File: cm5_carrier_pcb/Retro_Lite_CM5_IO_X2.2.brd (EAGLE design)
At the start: 82.7 x 91.3 mm, 317 parts, among them J1 5025700893, J10 5051100892, J11 1072TR, J12 5034802000, J13 5040500491, J14 5051100492, J2 SJ-43516-SMT, J4 5051100492, J5 685119136923, J6 5034802000, J7 105450-0101, J8 MDT320E01001, J9 5051103091, Q1 AO3400A, Q2 AO3400A, Q3 AO3400A, Q4 AO3400A, Q5 AO3400A, Q6 AO3400A, Q7 AO3400A, Q8 AO3400A, Q9 AO3400A, U10 UM3204QQFN14_3.5X3.5_UM3204_U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, U11 MAX17055ETB+T, U12 SY8089AAACSY8089AAAC_SGY-L, U13 UM3204QQFN14_3.5X3.5_UM3204_U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, U14 MCU-ATTINY84A-MU(QFN20), U16 TPS61160ADRVT, U18 TSIC_306_SOP-8, U19 SN74LVC1G17DCKR, U2 TPD4E05U06DQAR, U20 SN74LVC1G17DCKR, U21 TPS65987DDHRSHR, U22 TPD4E05U06DQAR, U23 TUSB546-DCIRNQT, U24 TPD4E05U06DQAR, U3 TPD4E05U06DQAR, U4 W25X05CLUXIGTR, U5 BQ24292I, U6 WM8960, U7 TPS61235PRWLT, U8 UM3204QQFN14_3.5X3.5_UM3204_U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, U9 UM3204QQFN14_3.5X3.5_UM3204_U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, Y1 ECS-3225MV-240-BN-TR, Y2 ECS-.327-12.5-12R-TR

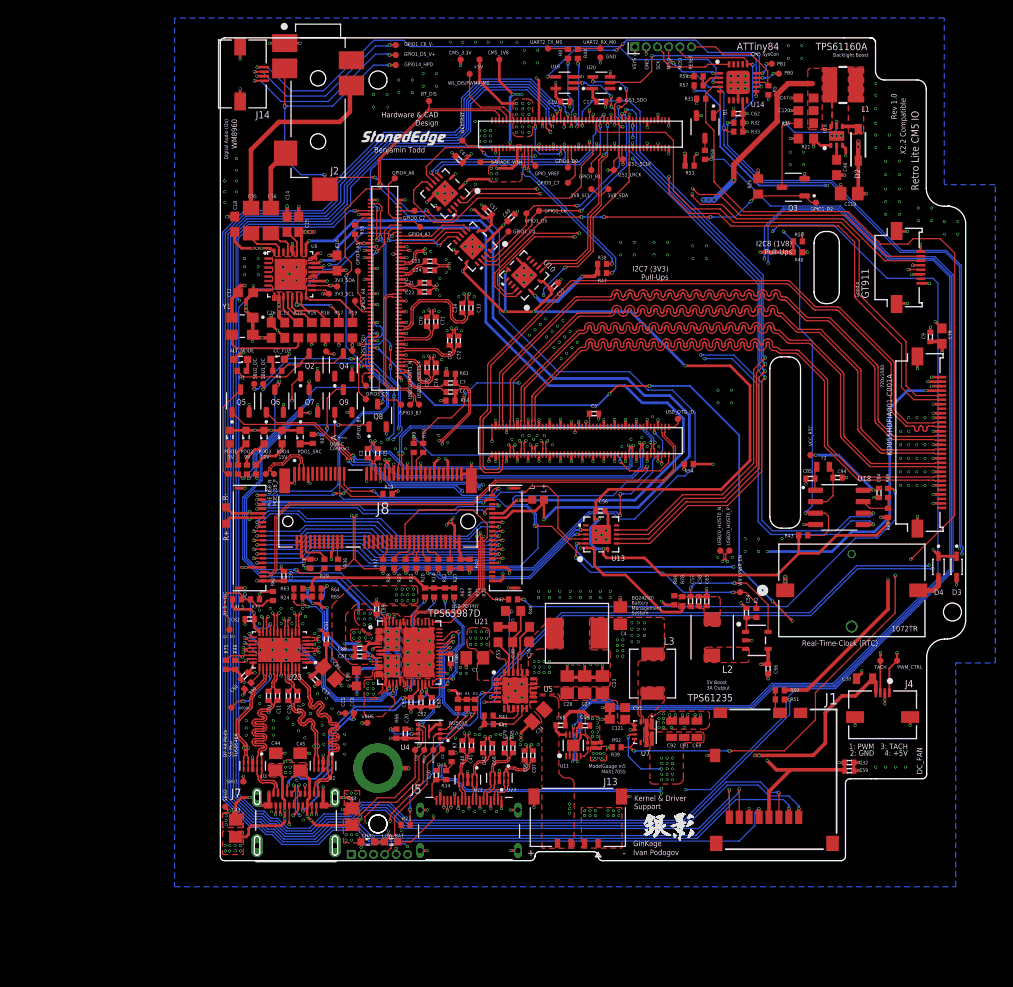
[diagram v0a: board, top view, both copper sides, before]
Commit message: Fix M.2 standoff hole size for 9774015243R
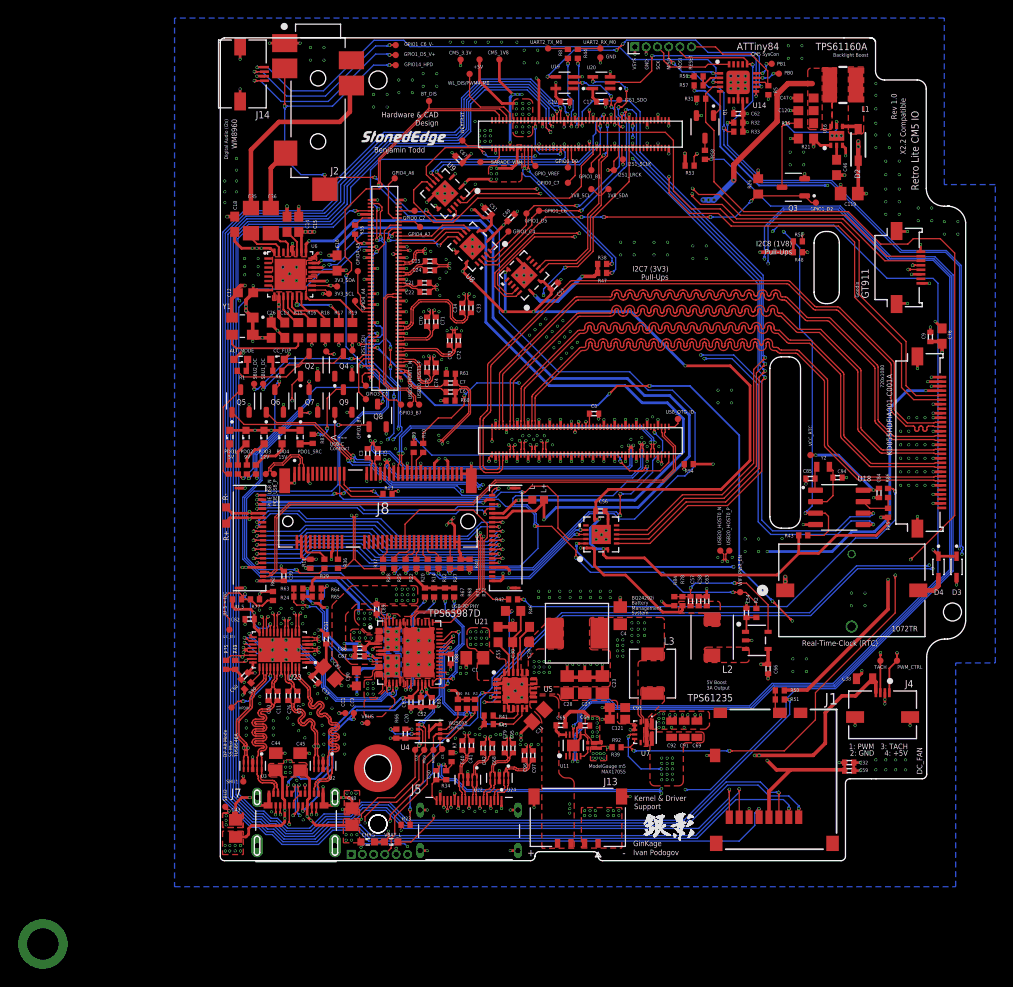
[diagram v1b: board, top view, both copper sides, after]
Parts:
- added H1: M2 x 1.5mm, Eagle_WA-SMSI (rev21a):WA-SMSI_9774015243
- moved U$7 42.0 mm to (-29.1, -12.8), flipped to the bottom
- moved R84 0.10 mm to (40.9, 25.2)
- renumbered LOW_BAT to VBAT_L
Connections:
- net GND: now also H1.1; no longer U$7.P$1
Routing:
- net GND: track 304.1 -> 300.5 mm, vias 554 -> 557

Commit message: Add files via upload
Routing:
- net GND: track 300.5 -> 303.5 mm, vias 557 -> 562

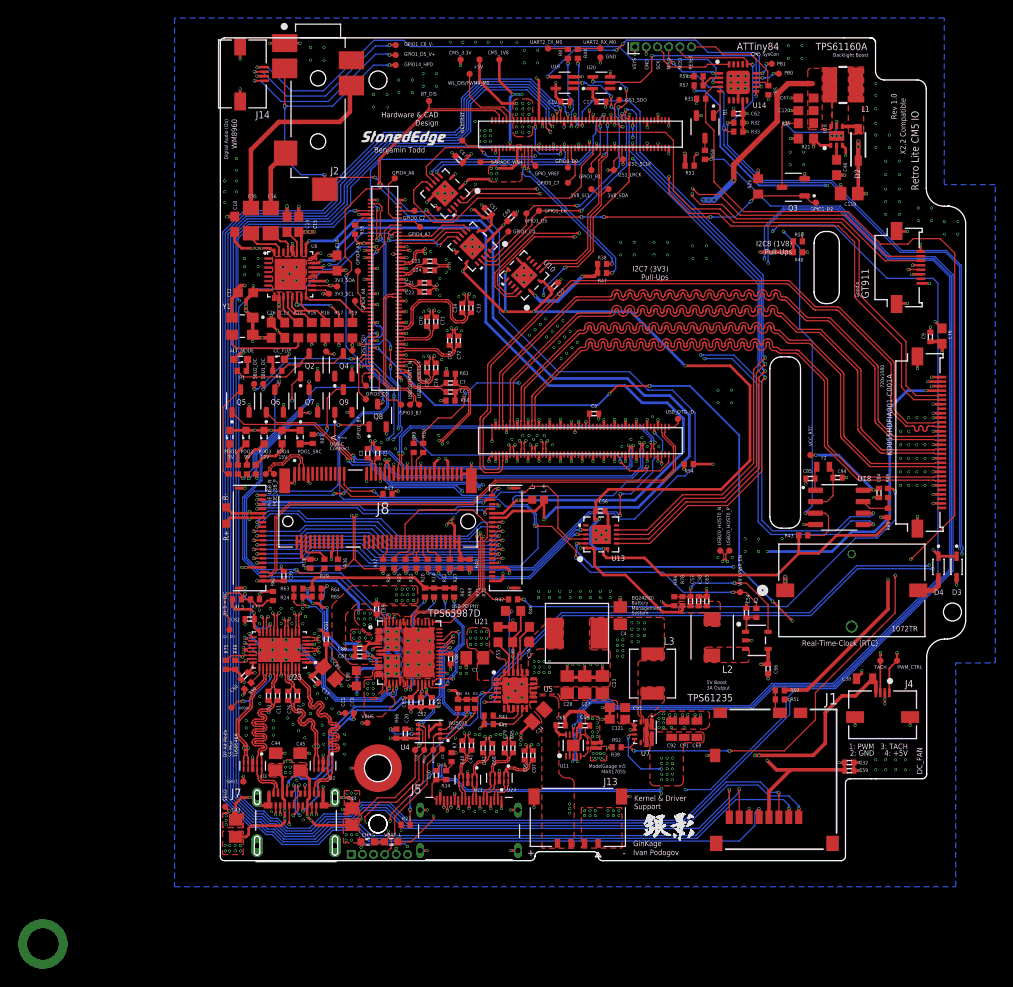
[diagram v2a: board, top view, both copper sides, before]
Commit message: Add BG_STAT, PG_GOOD pins to CM5 GPIOs
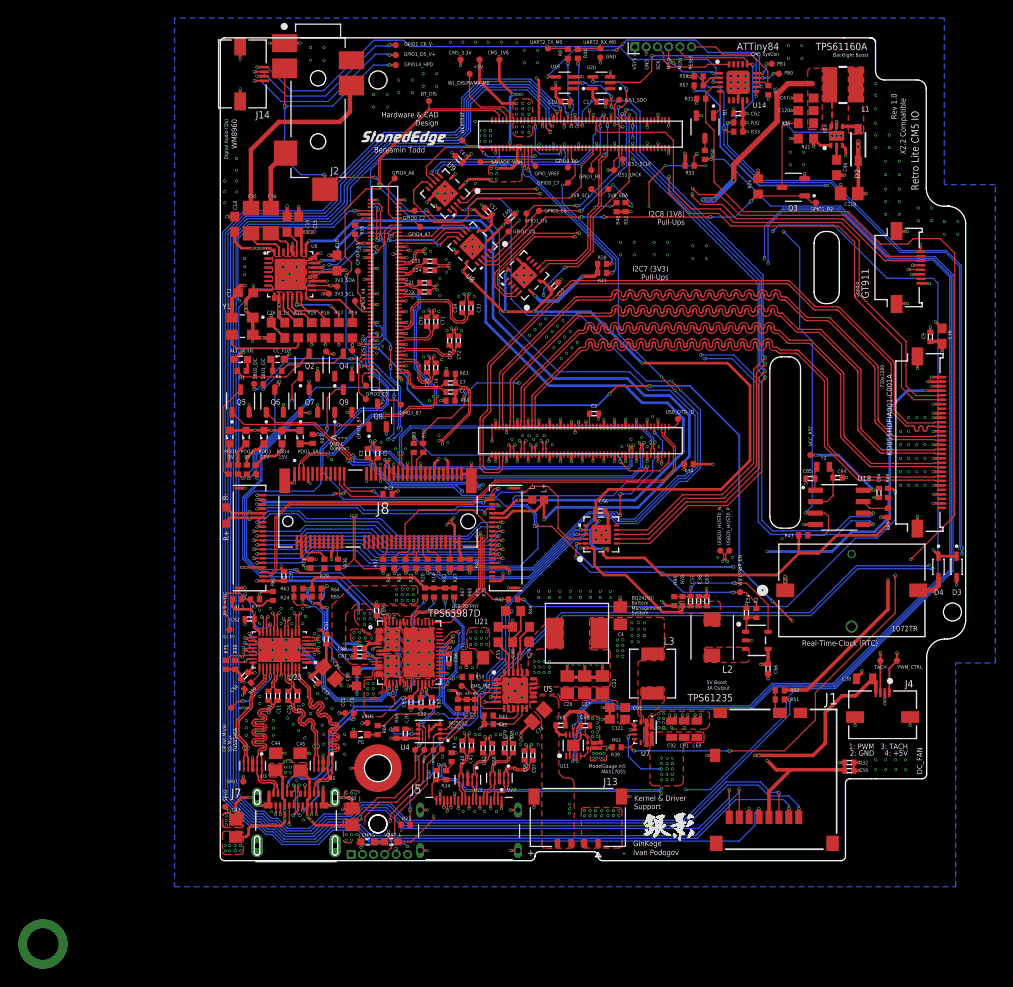
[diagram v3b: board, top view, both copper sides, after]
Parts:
- removed PCIE_USB_N, PCIE_USB_P, USB20_HOST1_N, USB20_HOST1_P: TPTP07R, testpad:TP07R
- added BMS_INT: TPTP07R, testpad:TP07R
- added PG: (no value), led:SML0603
- added R59: 4.7k, rcl:R0402
- added R69: 2.2k, rcl:R0402
- moved R48 20.7 mm to (34.5, 68.9), turned to 270 degrees
- moved R52 19.5 mm to (35.5, 68.9), turned to 270 degrees
- moved C88 0.20 mm to (15.9, 18.8)
- moved C89 0.20 mm to (7.89, 24.1)
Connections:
- removed net GPIO17_INT: R53.2, U11.8
- removed net GPIO1_A6_CAM1_E: U9.12
- removed net WIFI_USB_N: J8.5, PCIE_USB_N.TP
- removed net WIFI_USB_P: J8.3, PCIE_USB_P.TP
- new net BMS_INT: BMS_INT.TP, R59.2, U5.7
- new net BMS_PG: R69.1
- new net N$66: PG.C, R69.2
- net BMS_STAT: now also U9.12
- net GPIO0_C7: now also U5.3
- net GPIO1_C4: now also R53.2, U11.8
- net I2C8_SCL_M2: no longer R48.1
- net I2C8_SCL_M2_CAM: now also R48.1
- net I2C8_SDA_M2: no longer R52.1
- net I2C8_SDA_M2_CAM: now also R52.1
- net USB20_HOST1_D_N: now also J8.5; no longer USB20_HOST1_N.TP
- net USB20_HOST1_D_P: now also J8.3; no longer USB20_HOST1_P.TP
- net VSYS: now also PG.A, R59.1
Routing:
- net GPIO1_C4: track 3.02 -> 160.5 mm, vias 0 -> 7
- net GPIO17_INT: track 129.6 -> 0.00 mm, vias 3 -> 0
- net BMS_STAT: track 29.0 -> 118.2 mm, vias 2 -> 5
- net GPIO0_C7: track 4.36 -> 82.4 mm, vias 0 -> 4
- net USB20_HOST1_D_P: track 15.9 -> 34.3 mm, vias 0 -> 4
- net USB20_HOST1_D_N: track 16.3 -> 34.7 mm, vias 0 -> 4
- net BMS_PG: track 0.00 -> 15.1 mm, vias 0 -> 2
- net BMS_INT: track 0.00 -> 8.35 mm
- net WIFI_USB_N: track 7.09 -> 0.00 mm
- net CM5_1.8V(OUTPUT): track 124.1 -> 130.9 mm
- net I2C8_SCL_M2: track 70.8 -> 64.5 mm, vias 3 -> 2
- net WIFI_USB_P: track 6.34 -> 0.00 mm
- net I2C8_SDA_M2: track 71.2 -> 65.8 mm, vias 3 -> 2
- net I2C8_SDA_M2_CAM: track 19.6 -> 24.4 mm, vias 0 -> 2
- net I2S0_SCLK_TX: track 2.88 -> 0.00 mm, vias 1 -> 0
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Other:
- board text added: "720x1280"
- board text removed: "720x1080"
